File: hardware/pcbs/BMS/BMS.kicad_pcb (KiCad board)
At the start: 4 copper layers, 88.2 x 57.2 mm, 60 parts, among them J1 XT60-M, J2 XT60-F, J3 4-1971800-1, Q1 BSC014N04LSIATMA1, Q2 BSC014N04LSIATMA1, Q3 BSS84, SW1 CK_KMS2xxG, SW2 CK_KMS2xxG, SW3 CK_KMS2xxG, U1 BQ76920PW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

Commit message: Voltage supply of sEMG & ADC
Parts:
- removed the G*** at (147.8, 79.0)
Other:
- board text added: "BMS v0.1"

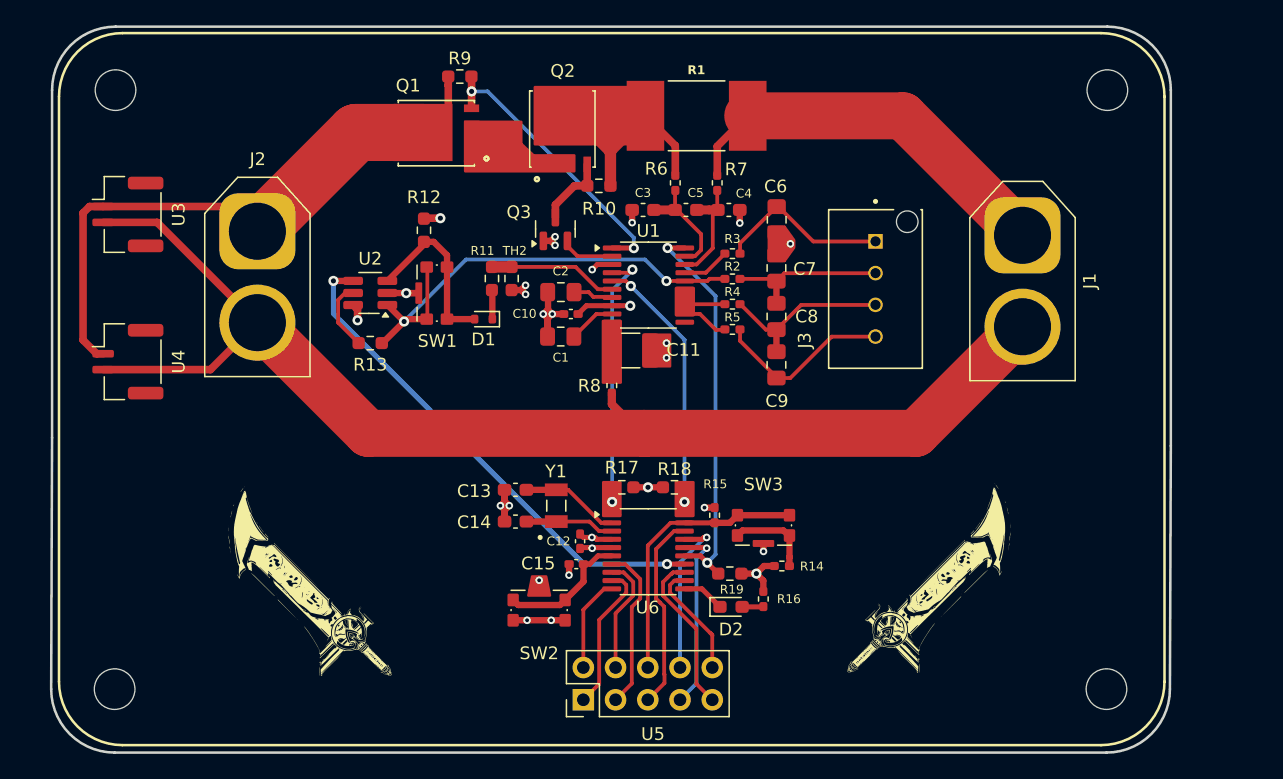
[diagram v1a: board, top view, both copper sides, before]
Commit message: BMS v0.2v + polishment of Vsupply  board
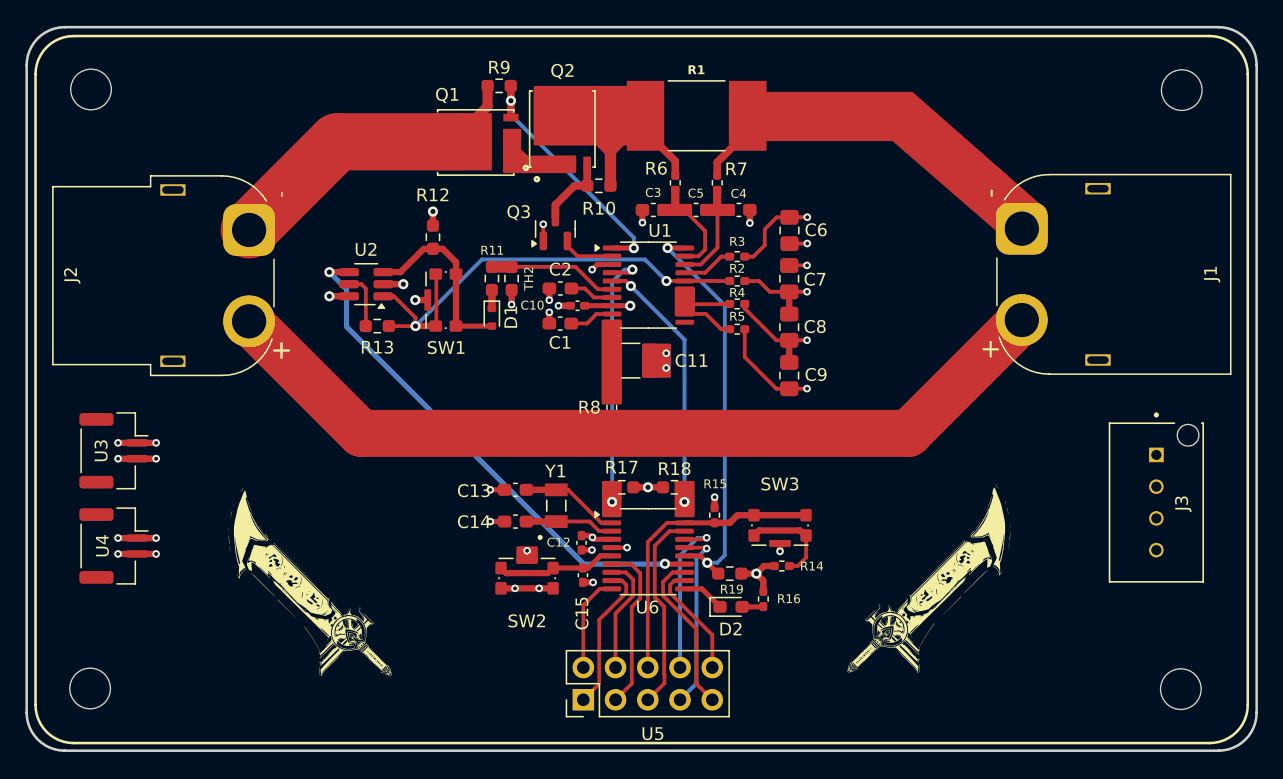
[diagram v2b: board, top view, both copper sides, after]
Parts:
- C1, C2: footprint Capacitor_SMD:C_0805_2012Metric_Pad1.18x1.45mm_HandSolder -> Capacitor_SMD:C_0603_1608Metric_Pad1.08x0.95mm_HandSolder
- J1: footprint Connector_AMASS:AMASS_XT60-M_1x02_P7.20mm_Vertical -> Connector_AMASS:AMASS_XT60PW-M_1x02_P7.20mm_Horizontal
- J2: footprint Connector_AMASS:AMASS_XT60-F_1x02_P7.20mm_Vertical -> Connector_AMASS:AMASS_XT60PW-F_1x02_P7.20mm_Horizontal
- U3, U4: footprint Connector_JST:JST_GH_BM02B-GHS-TBT_1x02-1MP_P1.25mm_Vertical -> Connector_JST:JST_GH_SM02B-GHS-TB_1x02-1MP_P1.25mm_Horizontal
- moved J3 27.8 mm to (191.9, 107.4)
- moved U3 18.7 mm to (109.8, 107.1)
- moved U4 14.6 mm to (109.8, 114.6)
- moved H2 5.86 mm to (193.9, 78.7)
- moved H4 5.86 mm to (193.8, 125.8)
- moved Q1 3.19 mm to (138.3, 82.8)
- moved R9 3.19 mm to (140.1, 78.3)
- moved SW2 2.69 mm to (142.3, 117.1)
- moved H1 1.93 mm to (108.0, 78.6)
- moved H3 1.93 mm to (107.9, 125.8)
- moved R8 1.72 mm to (149.0, 103.7)
- moved R13 1.45 mm to (130.5, 97.2)
- moved C6 1.31 mm to (163.0, 89.7)
- moved C7 1.31 mm to (163.0, 93.5)
- moved C8 1.31 mm to (163.0, 97.3)
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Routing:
- net PACK-: track 65.0 -> 30.4 mm, vias 23 -> 25
- net Net-(C6-Pad2): track 13.8 -> 42.2 mm, vias 0 -> 1
- net Net-(C7-Pad1): track 12.8 -> 40.9 mm, vias 0 -> 1
- net Net-(C8-Pad1): track 14.0 -> 41.4 mm, vias 0 -> 1
- net Net-(C9-Pad1): track 14.2 -> 40.9 mm, vias 0 -> 1
- net /BMS_GND: track 48.3 -> 66.1 mm, vias 0 -> 4
- net PACK+: track 102.2 -> 109.4 mm, vias 0 -> 4
- net +3.3V: track 71.8 -> 75.4 mm
- net Net-(Q1-G): track 22.9 -> 19.8 mm
- net Net-(U1-SRP): track 8.66 -> 6.10 mm
- net Net-(U1-SRN): track 8.81 -> 6.38 mm
- net Net-(Q2-D): track 17.2 -> 15.0 mm
- net Net-(U6-PF2): track 10.5 -> 8.88 mm
- net PA14: track 21.6 -> 23.0 mm
- net Net-(U2-DIR): track 5.48 -> 4.41 mm
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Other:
- board size 88.2 x 57.2 mm -> 96.9 x 57 mm
- board text added: "BMS v0.2"
- board text removed: "BMS v0.1"

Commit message: BMS v0.3 + main folder reconstruction
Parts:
- J3: footprint headers:XH_2.5mm -> Connector_JST:JST_XH_S4B-XH-A_1x04_P2.50mm_Horizontal
- U5: footprint Connector_PinHeader_2.54mm:PinHeader_2x05_P2.54mm_Vertical -> Connector_PinHeader_2.54mm:PinHeader_2x05_P2.54mm_Horizontal
- moved U5 10.5 mm to (156.9, 124.3), turned to -90 degrees
- moved J3 7.52 mm to (189.6, 114.5)
- moved U3 2.80 mm to (107.0, 107.1)
- moved U4 2.80 mm to (107.0, 114.6)
- moved H2 1.10 mm to (195.0, 78.7)
- moved H4 1.10 mm to (194.9, 125.8)
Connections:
- J3 pad 1: Net-(C6-Pad2) -> Net-(C9-Pad1)
- J3 pad 2: Net-(C7-Pad1) -> Net-(C8-Pad1)
- J3 pad 3: Net-(C8-Pad1) -> Net-(C7-Pad1)
- J3 pad 4: Net-(C9-Pad1) -> Net-(C6-Pad2)
- U5 pad 1: PA2 -> PA5
- U5 pad 10: PA5 -> PA2
- U5 pad 2: PA3 -> PA6
- U5 pad 3: PA0 -> PA12
- U5 pad 4: PA1 -> PA11
- U5 pad 5: PA13 -> PA14
- U5 pad 6: PA14 -> PA13
- U5 pad 7: PA11 -> PA1
- U5 pad 8: PA12 -> PA0
- U5 pad 9: PA6 -> PA3
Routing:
- net PACK+: track 109.4 -> 121.0 mm
- net /BMS_GND: track 66.1 -> 70.1 mm
- net Net-(C8-Pad1): track 41.4 -> 39.0 mm
- net Net-(C9-Pad1): track 40.9 -> 38.4 mm
- net Net-(C6-Pad2): track 42.2 -> 39.7 mm
- net Net-(C7-Pad1): track 40.9 -> 38.4 mm
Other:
- board text added: "BMS v0.3"
- board text removed: "BMS v0.2"
